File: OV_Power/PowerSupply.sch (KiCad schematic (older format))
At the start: 16 parts, among them J1 Kycon_kpjx-4s_shielded, J2 Conn_HDR_2x10_latching, J3 532530670, J6 CONN_HEADER_2.54X2_MOLEX_KK_S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, J7 CONN_HEADER_2.54X2_MOLEX_KK_S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, Q3 SZNUD3124LT1G, Q4 SZNUD3124LT1G, U7 LTC4416, U8 AOSD21307, U9 AOSD21307

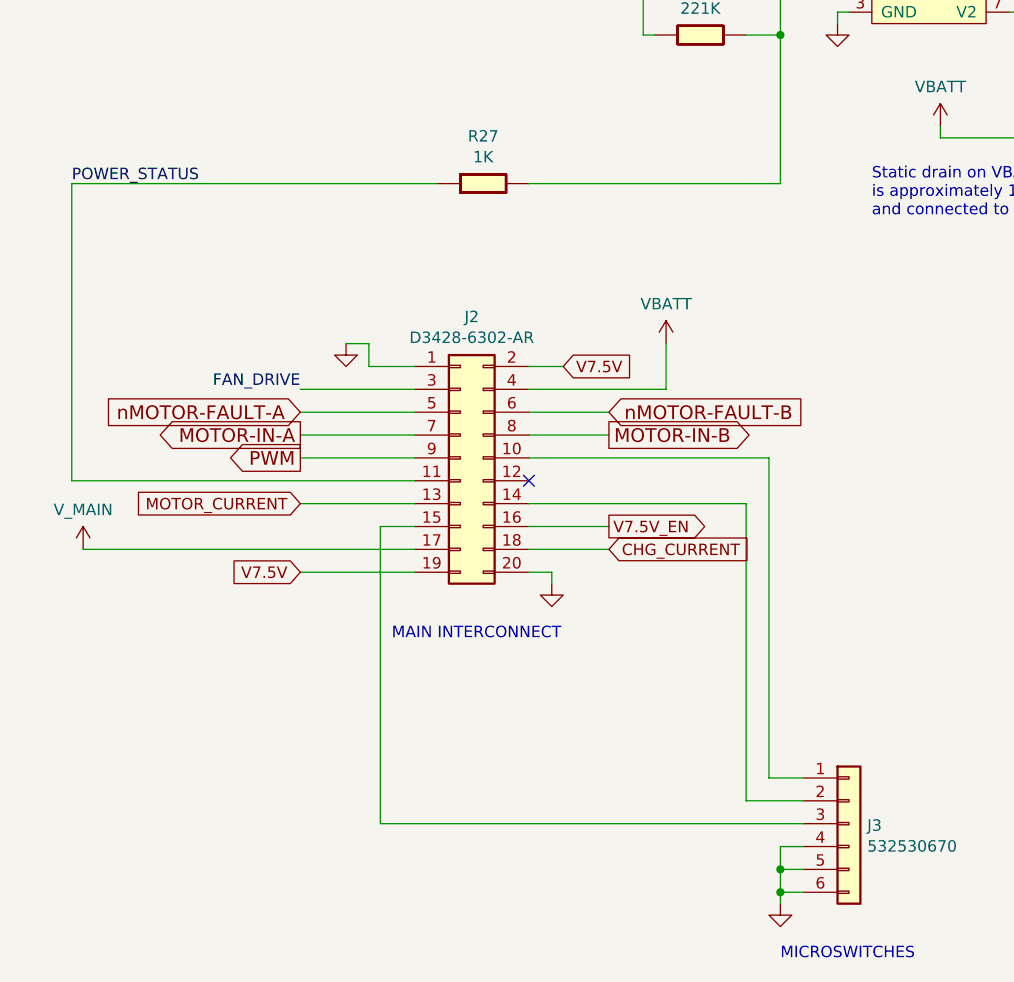
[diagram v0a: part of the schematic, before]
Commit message: Finally getting on with board routing, in TWO layers.  Warning, some things changed on the 20 pin interconnect.
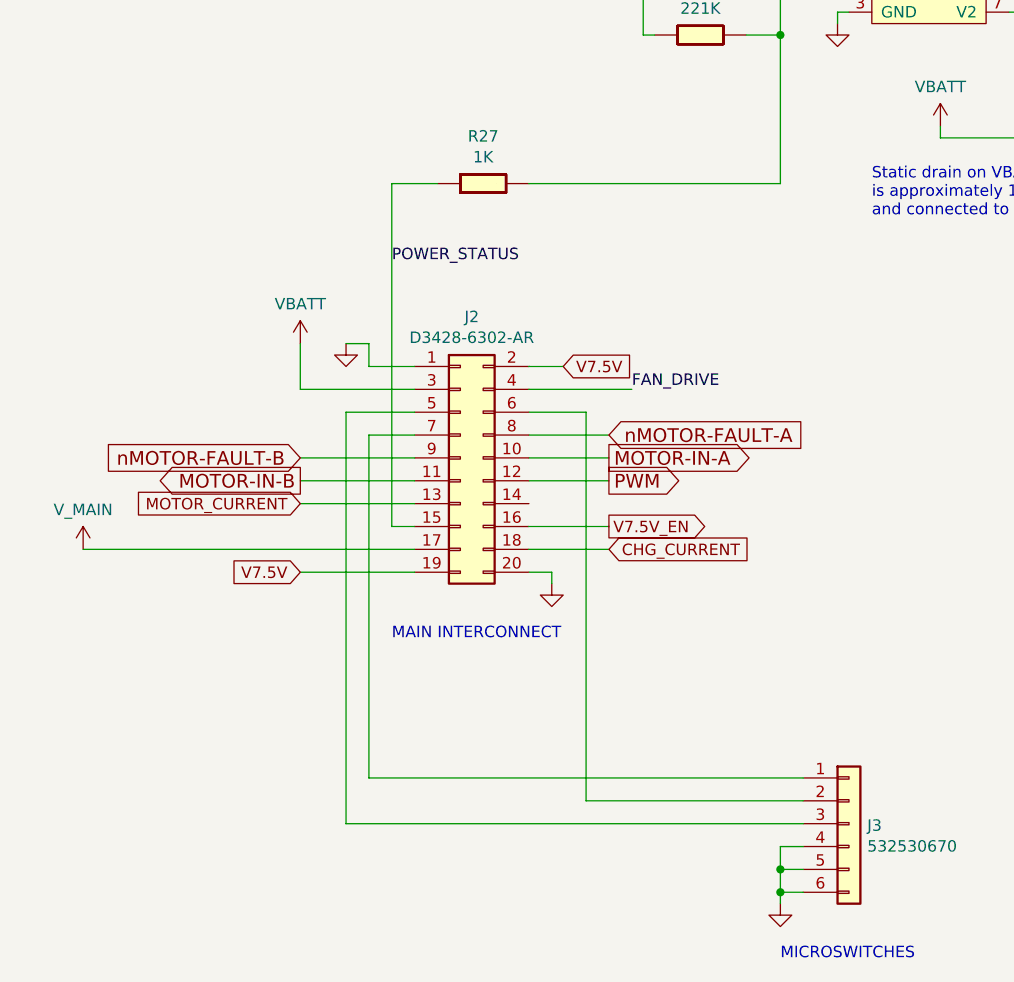
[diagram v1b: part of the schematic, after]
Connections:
- net FAN_DRIVE: now also J2.4 (Pin_4); no longer J2.3 (Pin_3)
- net MOTOR-IN-A: now also J2.10 (Pin_10); no longer J2.7 (Pin_7)
- net MOTOR-IN-B: now also J2.11 (Pin_11); no longer J2.8 (Pin_8)
- net POWER_STATUS: now also J2.15 (Pin_15); no longer J2.11 (Pin_11)
- net PWM: now also J2.12 (Pin_12); no longer J2.9 (Pin_9)
- net VBATT: now also J2.3 (Pin_3); no longer J2.4 (Pin_4)
- net nMOTOR-FAULT-A: now also J2.8 (Pin_8); no longer J2.5 (Pin_5)
- net nMOTOR-FAULT-B: now also J2.9 (Pin_9); no longer J2.6 (Pin_6)
- net at J3.1 (Pin_1): now also J2.7 (Pin_7); no longer J2.10 (Pin_10)
- net at J2.14 (Pin_14): no longer J3.2 (Pin_2)
- net at J3.3 (Pin_3): now also J2.5 (Pin_5); no longer J2.15 (Pin_15)
- new net: J2.6 (Pin_6), J3.2 (Pin_2)
- no-connect marks 2 -> 1
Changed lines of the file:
@@
 L OpenVent:VBATT #PWR032
 U 1 1 5FB6E37F
-P 3400 4500
-F 0 "#PWR032" H 3400 4350 50  0001 C CNN
-F 1 "VBATT" H 3400 4673 50  0000 C CNN
-F 2 "" H 3400 4500 50  0001 C CNN
-F 3 "" H 3400 4500 50  0001 C CNN
-	1    3400 4500
-	1    0    0    -1
-$EndComp
-Wire Wire Line
-	2800 4700 3400 4700
-Wire Wire Line
-	3400 4700 3400 4500
-Text GLabel 1800 5000 0    60   Output ~ 0
+P 1800 4500
+F 0 "#PWR032" H 1800 4350 50  0001 C CNN
+F 1 "VBATT" H 1800 4673 50  0000 C CNN
+F 2 "" H 1800 4500 50  0001 C CNN
+F 3 "" H 1800 4500 50  0001 C CNN
+	1    1800 4500
+	1    0    0    -1
+$EndComp
+Wire Wire Line
+	1800 4700 1800 4500
+Text GLabel 3150 5100 2    60   Output ~ 0
 PWM
-Text GLabel 1800 4900 0    60   Output ~ 0
+Text GLabel 3150 5000 2    60   Output ~ 0
 MOTOR-IN-A
-Text GLabel 3150 4900 2    60   Output ~ 0
+Text GLabel 1800 5100 0    60   Output ~ 0
 MOTOR-IN-B
-Text GLabel 1800 4800 0    60   Input ~ 0
+Text GLabel 3150 4900 2    60   Input ~ 0
 nMOTOR-FAULT-A
-Text GLabel 3150 4800 2    60   Input ~ 0
+Text GLabel 1800 5000 0    60   Input ~ 0
 nMOTOR-FAULT-B
-Wire Wire Line
-	1800 4800 2300 4800
-Wire Wire Line
-	2800 4800 3150 4800
-Wire Wire Line
-	1800 4900 2300 4900
-Wire Wire Line
-	3150 4900 2800 4900
-Wire Wire Line
-	2300 5000 1800 5000
 Text GLabel 3150 5400 2    50   Input ~ 0
 CHG_CURRENT
@@
 	3900 6900 3900 6950
 Wire Wire Line
-	4000 6600 2150 6600
-Wire Wire Line
-	2150 6600 2150 5300
-Wire Wire Line
-	2150 5300 2300 5300
-Wire Wire Line
-	4000 6500 3750 6500
-Wire Wire Line
-	3750 6500 3750 5200
-Wire Wire Line
-	3750 5200 2800 5200
-Wire Wire Line
-	2800 5000 3850 5000
-Wire Wire Line
-	3850 5000 3850 6400
-Wire Wire Line
-	3850 6400 4000 6400
+	4000 6600 2000 6600
 Text Notes 2200 5800 0    50   ~ 0
 MAIN INTERCONNECT
@@
 Wire Wire Line
 	8650 4800 8750 4800
-Wire Wire Line
-	2300 4700 1800 4700
-Text Label 1800 4700 2    50   ~ 0
+Text Label 3250 4700 0    50   ~ 0
 FAN_DRIVE
 Wire Wire Line
@@
 Connection ~ 3900 3150
 Wire Wire Line
-	2400 3800 800  3800
-Wire Wire Line
-	800  3800 800  5100
-Wire Wire Line
-	800  5100 2300 5100
-Text Label 800  3800 0    50   ~ 0
+	2400 3800 2200 3800
+Text Label 2200 4150 0    50   ~ 0
 POWER_STATUS
 Wire Wire Line
@@
 	3150 5400 2800 5400
 NoConn ~ 4200 2450
-NoConn ~ 2800 5100
 $Comp
 L OpenVent:VIN_12V #PWR0101
@@
 Wire Wire Line
 	1400 1800 1400 1900
+Wire Wire Line
+	3250 4700 2800 4700
+Wire Wire Line
+	2300 4700 1800 4700
+Wire Wire Line
+	2300 4800 2000 4800
+Wire Wire Line
+	2000 4800 2000 6600
+Wire Wire Line
+	3050 6500 3050 4800
+Wire Wire Line
+	3050 4800 2800 4800
+Wire Wire Line
+	3050 6500 4000 6500
+Wire Wire Line
+	2100 6400 2100 4900
+Wire Wire Line
+	2100 4900 2300 4900
+Wire Wire Line
+	3150 4900 2800 4900
+Wire Wire Line
+	2300 5000 1800 5000
+Wire Wire Line
+	3150 5000 2800 5000
+Wire Wire Line
+	2300 5100 1800 5100
+Wire Wire Line
+	3150 5100 2800 5100
+Wire Wire Line
+	2300 5300 2200 5300
+Wire Wire Line
+	2200 5300 2200 3800
+Wire Wire Line
+	2100 6400 4000 6400
 $EndSCHEMATC

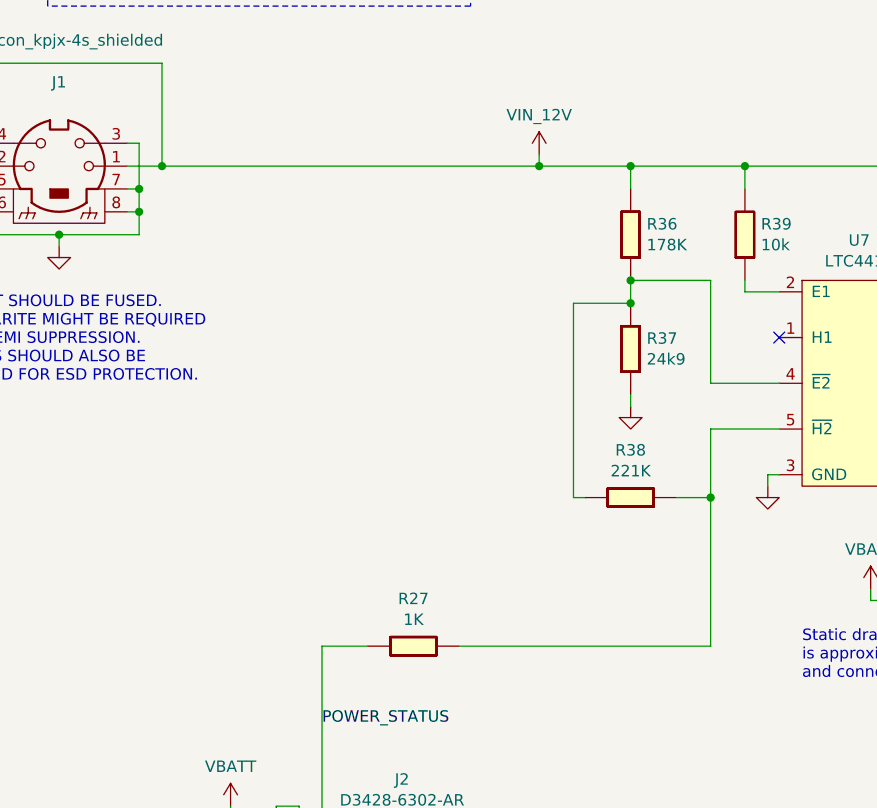
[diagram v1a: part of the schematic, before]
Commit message: Slight change to schemo per Rick's suggestion, also generated the real BOM.  Gerbers updated, should be ready for production.
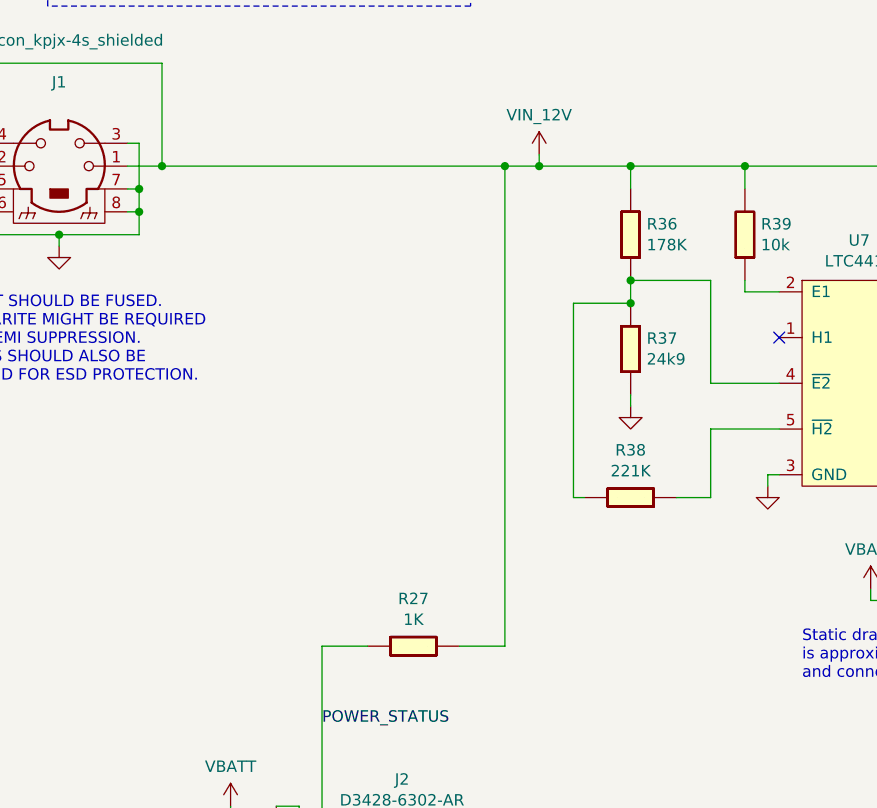
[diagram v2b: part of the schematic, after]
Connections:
- net VIN_12V: now also R27.2
- net at R38.1, U7.5 (~H2~): no longer R27.2
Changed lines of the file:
@@
 FAN_DRIVE
 Wire Wire Line
-	1500 1700 3150 1700
+	1500 1700 3000 1700
 Connection ~ 1500 1700
 Connection ~ 3550 1700
@@
 	1    0    0    -1
 $EndComp
-Wire Wire Line
-	3900 3150 3900 3800
-Wire Wire Line
-	3900 3800 2800 3800
-Connection ~ 3900 3150
 Wire Wire Line
 	2400 3800 2200 3800
@@
 Wire Wire Line
 	2100 6400 4000 6400
+Wire Wire Line
+	2800 3800 3000 3800
+Wire Wire Line
+	3000 3800 3000 1700
+Connection ~ 3000 1700
+Wire Wire Line
+	3000 1700 3150 1700
 $EndSCHEMATC
